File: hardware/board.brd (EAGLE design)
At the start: 53 x 30 mm, 47 parts, among them IC1 0915BM15A0001, J1 U.FL, U3 BLE113-A, X1 24MHz 8pF 10ppm -20C +70C, X3 MINI-USB-UX60-MB-5ST

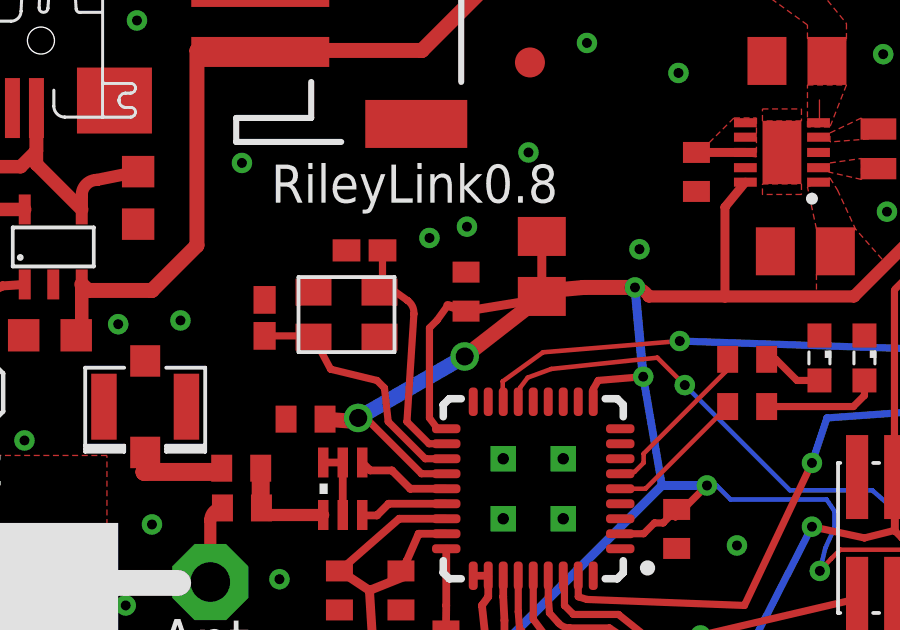
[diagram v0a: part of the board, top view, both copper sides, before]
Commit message: Fix bad trace under supply cap
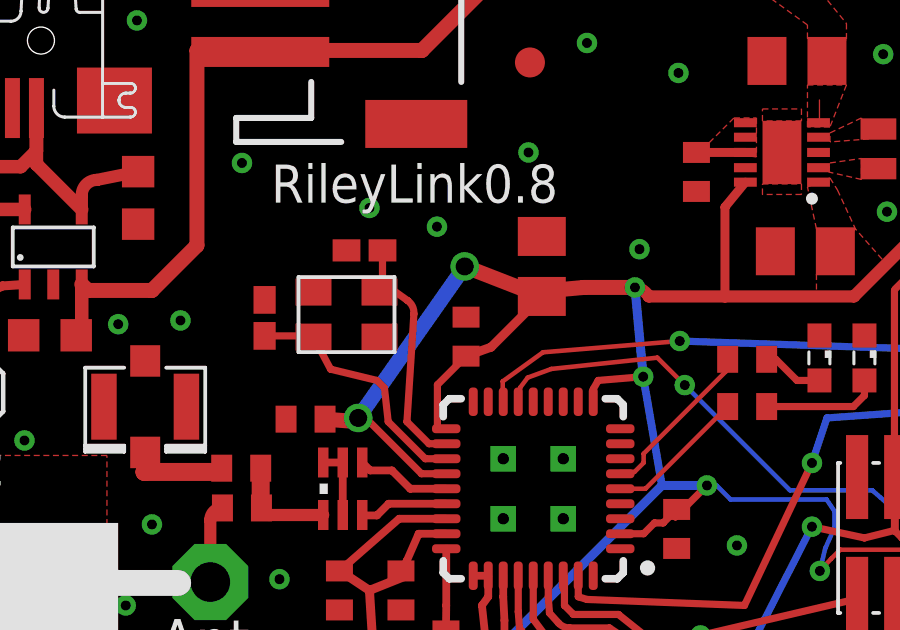
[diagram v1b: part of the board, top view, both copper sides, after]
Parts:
- moved C12 1.50 mm to (22.0, 14.0)
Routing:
- net VDD: track 127.5 -> 125.2 mm
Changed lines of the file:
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@@
 <?xml version="1.0" encoding="utf-8"?>
 <!DOCTYPE eagle SYSTEM "eagle.dtd">
-<eagle version="7.5.0">
+<eagle version="7.7.0">
 <drawing>
 <settings>
@@
 <setting verticaltext="up"/>
 </settings>
-<grid distance="0.5" unitdist="mm" unit="mm" style="lines" multiple="1" display="yes" altdistance="0.000393700787" altunitdist="inch" altunit="inch"/>
+<grid distance="0.05" unitdist="mm" unit="mm" style="lines" multiple="1" display="no" altdistance="0.000393700787" altunitdist="inch" altunit="inch"/>
 <layers>
 <layer number="1" name="Top" color="4" fill="1" visible="yes" active="yes"/>
@@
 <layer number="27" name="tValues" color="7" fill="1" visible="no" active="yes"/>
 <layer number="28" name="bValues" color="7" fill="1" visible="no" active="yes"/>
-<layer number="29" name="tStop" color="7" fill="3" visible="no" active="yes"/>
+<layer number="29" name="tStop" color="7" fill="3" visible="yes" active="yes"/>
 <layer number="30" name="bStop" color="7" fill="6" visible="no" active="yes"/>
-<layer number="31" name="tCream" color="7" fill="4" visible="no" active="yes"/>
+<layer number="31" name="tCream" color="7" fill="4" visible="yes" active="yes"/>
 <layer number="32" name="bCream" color="7" fill="5" visible="no" active="yes"/>
 <layer number="33" name="tFinish" color="6" fill="3" visible="no" active="yes"/>
@@
 <attribute name="VALUE" x="26.4" y="15.665" size="1.27" layer="27" rot="R90"/>
 </element>
-<element name="C12" library="rcl" package="C0402" value="0.1uF" x="21.97" y="15.46" smashed="yes" rot="R90">
-<attribute name="VALUE" x="23.875" y="14.825" size="1.27" layer="27" rot="R90"/>
+<element name="C12" library="rcl" package="C0402" value="0.1uF" x="21.97" y="13.96" smashed="yes" rot="R90">
+<attribute name="VALUE" x="23.875" y="13.325" size="1.27" layer="27" rot="R90"/>
 </element>
 <element name="C13" library="rcl" package="C0402" value="0.1uF" x="16.62" y="11.21" smashed="yes" rot="R180">
@@
 <via x="49" y="1" extent="1-16" drill="0.3302" diameter="0.4064"/>
 <via x="41.375" y="9.75" extent="1-16" drill="0.3302" diameter="0.4064"/>
-<via x="20.75" y="17.25" extent="1-16" drill="0.3302" diameter="0.4064"/>
+<via x="18.75" y="18.25" extent="1-16" drill="0.3302" diameter="0.4064"/>
 <via x="10.375" y="14.375" extent="1-16" drill="0.3302" diameter="0.4064"/>
 <via x="14.5" y="19.75" extent="1-16" drill="0.3302" diameter="0.4064"/>
@@
 <via x="16.125" y="3.25" extent="1-16" drill="0.3302" diameter="0.4064"/>
 <via x="27.75" y="16.875" extent="1-16" drill="0.3302" diameter="0.4064"/>
-<via x="22" y="17.625" extent="1-16" drill="0.3302" diameter="0.4064"/>
+<via x="21" y="17.625" extent="1-16" drill="0.3302" diameter="0.4064"/>
 <contactref element="C14" pad="1"/>
 <polygon width="0.01" layer="1" thermals="no">
@@
 <via x="33.7626" y="6.1508" extent="1-16" drill="0.3302"/>
 <wire x1="21.31" y1="10.89" x2="21.015" y2="10.89" width="0.24" layer="1"/>
-<wire x1="21.015" y1="10.89" x2="20.75" y2="11.25" width="0.24" layer="1"/>
 <wire x1="21.31" y1="9.39" x2="20.485" y2="9.39" width="0.24" layer="1"/>
 <wire x1="20.485" y1="9.39" x2="18.75" y2="11.125" width="0.24" layer="1"/>
@@
 <wire x1="37.625" y1="22.914578125" x2="37.625" y2="18.5134" width="0.3" layer="1"/>
 <wire x1="37.625" y1="18.5134" x2="37.4356" y2="18.324" width="0.3" layer="1"/>
-<wire x1="20.75" y1="11.25" x2="20.75" y2="14.25" width="0.24" layer="1"/>
-<wire x1="20.75" y1="14.25" x2="21" y2="14.5" width="0.24" layer="1"/>
-<wire x1="21" y1="14.5" x2="21.36" y2="15" width="0.24" layer="1"/>
-<wire x1="21.97" y1="14.81" x2="23.805" y2="15.11" width="0.3" layer="1"/>
-<wire x1="23.805" y1="15.11" x2="24.495" y2="15.3" width="0.3" layer="1"/>
+<wire x1="21.97" y1="13.31" x2="22.805" y2="13.61" width="0.3" layer="1"/>
+<wire x1="22.805" y1="13.61" x2="24.495" y2="15.3" width="0.3" layer="1"/>
 <wire x1="24.795" y1="15.5" x2="24.495" y2="15.3" width="0.3" layer="1"/>
-<wire x1="24.495" y1="15.3" x2="24.495" y2="17.6174875" width="0.3" layer="1"/>
-<wire x1="24.495" y1="17.6174875" x2="24.4874875" y2="17.625" width="0.3" layer="1"/>
-<wire x1="21.36" y1="15" x2="21.97" y2="14.81" width="0.3" layer="1"/>
 <wire x1="27.6" y1="15.6" x2="27.6140125" y2="15.6140125" width="0.4064" layer="1"/>
 <wire x1="27.6140125" y1="15.6140125" x2="28.063025" y2="15.3" width="0.4064" layer="1" curve="-45"/>
@@
 <wire x1="24.795" y1="15.5" x2="25.895" y2="15.6" width="0.5" layer="1"/>
 <wire x1="25.895" y1="15.6" x2="27.6" y2="15.6" width="0.5" layer="1"/>
-<wire x1="18.375" y1="11.25" x2="21.925" y2="13.3" width="0.5" layer="16"/>
-<wire x1="21.925" y1="13.3" x2="24.495" y2="15.3" width="0.5" layer="1"/>
+<wire x1="18.375" y1="11.25" x2="21.925" y2="16.3" width="0.5" layer="16"/>
+<wire x1="21.925" y1="16.3" x2="24.495" y2="15.3" width="0.5" layer="1"/>
 <via x="18.375" y="11.25" extent="1-16" drill="0.6"/>
-<via x="21.925" y="13.3" extent="1-16" drill="0.6"/>
+<via x="21.925" y="16.3" extent="1-16" drill="0.6"/>
+<wire x1="21.015" y1="10.89" x2="21.015" y2="12.355" width="0.24" layer="1"/>
+<wire x1="21.015" y1="12.355" x2="21.97" y2="13.31" width="0.24" layer="1"/>
 </signal>
 <signal name="N$3">
